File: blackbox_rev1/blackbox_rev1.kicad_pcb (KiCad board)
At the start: 2 copper layers, 16 parts, among them J1 RJ45_LED_Shielded, J2 Molex_uF_SV_06, SW1 SW_Push, SW2 SW_Push, U1 Teensy4.1_DEV-16771, U2 TSR1-2433

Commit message: finish layout design
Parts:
- added J3: Conn_02x08_Counter_Clockwise, blackbox_rev1:timerLED, F.Cu at (89.5, 92.7)
- moved SW1 28.7 mm to (124.2, 95.2)
- moved SW2 28.7 mm to (133.9, 95.2)
- moved C1 22.2 mm to (99.9, 59.9), turned to 0 degrees
- moved C2 14.6 mm to (104.6, 66.6), turned to -90 degrees
- moved C3 9.42 mm to (101.9, 66.6), turned to -90 degrees
- moved U2 8.05 mm to (90.4, 64.0)
- moved Conn1 8.02 mm to (79.2, 57.9)
- moved D3 7.75 mm to (99.7, 70.1), turned to 180 degrees
- moved R3 7.34 mm to (98.8, 66.7)
- moved R1 6.58 mm to (88.8, 70.1), turned to 180 degrees
- moved D1 6.16 mm to (93.0, 70.1), turned to 180 degrees
- moved Conn2 5.11 mm to (62.2, 74.2)
- moved J2 3.11 mm to (112.3, 67.9)
- moved J1 2.77 mm to (139.2, 61.8)
- moved C4 2.39 mm to (113.3, 55.7)
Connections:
- C2 pad 1: +3V3 -> +5V
- C3 pad 1: +3V3 -> +5V
- R3 pad 2: +3V3 -> +5V
- U1 pad 0: Display_A -> Display_D1_Low
- U1 pad 1: Display_B -> Display_D2_Low
- U1 pad 10: unconnected-(U1-Pad10) -> Display_D3_Low
- U1 pad 11: unconnected-(U1-Pad11) -> Display_D4_Low
- U1 pad 2: Display_C -> Display_D
- U1 pad 24: Display_D1_Low -> unconnected-(U1-Pad24)
- U1 pad 25: Display_D2_Low -> unconnected-(U1-Pad25)
- U1 pad 26: Display_D3_Low -> unconnected-(U1-Pad26)
- U1 pad 27: Display_D4_Low -> unconnected-(U1-Pad27)
- U1 pad 28: unconnected-(U1-Pad28) -> Sw_Hour
- U1 pad 29: unconnected-(U1-Pad29) -> Sw_Min
- U1 pad 3: Display_D -> Display_B
- U1 pad 4: Display_E -> Display_G
- U1 pad 5: Display_F -> Display_A
- U1 pad 6: Display_G -> Display_C
- U1 pad 7: Sw_Hour -> Clock_SquareWave
- U1 pad 8: Sw_Min -> Display_F
- U1 pad 9: unconnected-(U1-Pad9) -> Display_E
- U1 pad VIN: unconnected-(U1-PadVIN) -> +5V
- U2 pad 3: +3V3 -> +5V
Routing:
- net +3V3: track 0.00 -> 85.4 mm
- net +5V: track 0.00 -> 36.6 mm
- net Net-(C4-Pad2): track 0.00 -> 36.1 mm, vias 0 -> 1
- net +36V: track 0.00 -> 29.9 mm
- net Display_D1_Low: track 0.00 -> 17.4 mm
- net Display_D2_Low: track 0.00 -> 17.3 mm
- net Display_D: track 0.00 -> 17.1 mm
- net Display_D3_Low: track 0.00 -> 16.5 mm
- net Display_E: track 0.00 -> 16.3 mm
- net Net-(J1-Pad10): track 0.00 -> 16.2 mm
- net Display_D4_Low: track 0.00 -> 15.7 mm
- net Net-(C4-Pad1): track 0.00 -> 14.9 mm
- net Sw_Min: track 0.00 -> 12.3 mm
- net Sw_Hour: track 0.00 -> 12.3 mm
- net Net-(J1-Pad3): track 0.00 -> 9.81 mm
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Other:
- board outline added: 83.8 x 53.3 mm
- board text added: "BlackBox Board,2023 Rev1 Mars Rover Design Team Sanfan Liu"

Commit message: switch 3v3 oki to 5v
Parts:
- moved D3 5.84 mm to (105.5, 70.1)
- moved R3 5.84 mm to (104.6, 66.7)
- moved C2 5.59 mm to (99.1, 66.6)
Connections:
- SW1 pad 1: +3V3 -> GND
- SW2 pad 1: +3V3 -> GND
- U1 pad 3.3V_1: +3V3 -> Net-(U1-Pad3.3V_1)
- U1 pad 3.3V_2: +3V3 -> Net-(U1-Pad3.3V_1)
- U1 pad 3.3V_3: +3V3 -> Net-(U1-Pad3.3V_1)
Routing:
- net +3V3: track 85.4 -> 0.00 mm
- net Net-(U1-Pad3.3V_1): track 0.00 -> 55.8 mm
- net GND: track 0.00 -> 20.7 mm, vias 3 -> 7
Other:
- board text added: "36V"
- board text added: "5V"
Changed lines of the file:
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@@
   (net 1 "+36V")
   (net 2 "GND")
-  (net 3 "+3V3")
+  (net 3 "Net-(U1-Pad3.3V_1)")
   (net 4 "Net-(C4-Pad1)")
   (net 5 "Net-(C4-Pad2)")
@@
   )
   (footprint "LED_SMD:LED_0603_1608Metric_Pad1.05x0.95mm_HandSolder" (layer "F.Cu")
-    (at 99.681 70.104 180)
+    (at 105.523 70.104 180)
     (descr "LED SMD 0603 (1608 Metric), square (rectangular) end terminal, IPC_7351 nominal, (Body size source: http://www.tortai-tech.com/upload/download/2011102023233369053.pdf), generated with kicad-footprint-generator")
     (tags "LED handsolder")
@@
   )
   (footprint "Resistor_SMD:R_0603_1608Metric_Pad0.98x0.95mm_HandSolder" (layer "F.Cu")
-    (at 98.806 66.6985 90)
+    (at 104.648 66.6985 90)
     (descr "Resistor SMD 0603 (1608 Metric), square (rectangular) end terminal, IPC_7351 nominal with elongated pad for handsoldering. (Body size source: IPC-SM-782 page 72, https://www.pcb-3d.com/wordpress/wp-content/uploads/ipc-sm-782a_amendment_1_and_2.pdf), generated with kicad-footprint-generator")
     (tags "resistor handsolder")
@@
     (fp_circle (center 0 0) (end 1.25 0) (layer "F.Fab") (width 0.1) (fill none))
     (pad "1" smd rect (at -3.6 -1.5 180) (size 1.6 1.4) (layers "F.Cu" "F.Paste" "F.Mask")
-      (net 3 "+3V3") (pinfunction "1") (pintype "passive"))
+      (net 2 "GND") (pinfunction "1") (pintype "passive"))
     (pad "1" smd rect (at 3.6 -1.5 180) (size 1.6 1.4) (layers "F.Cu" "F.Paste" "F.Mask")
-      (net 3 "+3V3") (pinfunction "1") (pintype "passive"))
+      (net 2 "GND") (pinfunction "1") (pintype "passive"))
     (pad "2" smd rect (at 3.6 1.5 180) (size 1.6 1.4) (layers "F.Cu" "F.Paste" "F.Mask")
       (net 16 "Sw_Hour") (pinfunction "2") (pintype "passive"))
@@
   )
   (footprint "Capacitor_SMD:C_0603_1608Metric_Pad1.08x0.95mm_HandSolder" (layer "F.Cu")
-    (at 104.648 66.6485 -90)
+    (at 99.06 66.6485 -90)
     (descr "Capacitor SMD 0603 (1608 Metric), square (rectangular) end terminal, IPC_7351 nominal with elongated pad for handsoldering. (Body size source: IPC-SM-782 page 76, https://www.pcb-3d.com/wordpress/wp-content/uploads/ipc-sm-782a_amendment_1_and_2.pdf), generated with kicad-footprint-generator")
     (tags "capacitor handsolder")
@@
     (fp_circle (center 0 0) (end 1.25 0) (layer "F.Fab") (width 0.1) (fill none))
     (pad "1" smd rect (at -3.6 -1.5 180) (size 1.6 1.4) (layers "F.Cu" "F.Paste" "F.Mask")
-      (net 3 "+3V3") (pinfunction "1") (pintype "passive"))
+      (net 2 "GND") (pinfunction "1") (pintype "passive"))
     (pad "1" smd rect (at 3.6 -1.5 180) (size 1.6 1.4) (layers "F.Cu" "F.Paste" "F.Mask")
-      (net 3 "+3V3") (pinfunction "1") (pintype "passive"))
+      (net 2 "GND") (pinfunction "1") (pintype "passive"))
     (pad "2" smd rect (at -3.6 1.5 180) (size 1.6 1.4) (layers "F.Cu" "F.Paste" "F.Mask")
       (net 17 "Sw_Min") (pinfunction "2") (pintype "passive"))
@@
       (net 49 "Display_B") (pinfunction "LRCLK2") (pintype "bidirectional"))
     (pad "3.3V_1" thru_hole circle locked (at 57.15 43.18) (size 1.308 1.308) (drill 0.8) (layers *.Cu *.Mask)
-      (net 3 "+3V3") (pinfunction "3.3V") (pintype "power_in"))
+      (net 3 "Net-(U1-Pad3.3V_1)") (pinfunction "3.3V") (pintype "power_in"))
     (pad "3.3V_2" thru_hole circle locked (at 26.67 27.94) (size 1.308 1.308) (drill 0.8) (layers *.Cu *.Mask)
-      (net 3 "+3V3") (pinfunction "3.3V") (pintype "power_in"))
+      (net 3 "Net-(U1-Pad3.3V_1)") (pinfunction "3.3V") (pintype "power_in"))
     (pad "3.3V_3" thru_hole circle locked (at 67.31 38.1) (size 1.308 1.308) (drill 0.8) (layers *.Cu *.Mask)
-      (net 3 "+3V3") (pinfunction "3.3V") (pintype "power_in"))
+      (net 3 "Net-(U1-Pad3.3V_1)") (pinfunction "3.3V") (pintype "power_in"))
     (pad "4" thru_hole circle locked (at 34.29 43.18) (size 1.308 1.308) (drill 0.8) (layers *.Cu *.Mask)
       (net 34 "Display_G") (pinfunction "BCLK2") (pintype "bidirectional"))
@@
     (effects (font (size 0.95 0.95) (thickness 0.15)) (justify left))
   )
+  (gr_text "5V" (at 102.616 70.104) (layer "F.SilkS")
+    (effects (font (size 1 1) (thickness 0.15)))
+  )
+  (gr_text "36V" (at 96.266 70.104) (layer "F.SilkS")
+    (effects (font (size 1 1) (thickness 0.15)))
+  )
   (dimension (type aligned) (layer "Dwgs.User")
     (pts (xy 140.97 52.324) (xy 140.97 105.664))
@@
   (segment (start 89.408 59.944) (end 99.854 59.944) (width 0.762) (layer "F.Cu") (net 1))
   (segment (start 87.884 65.786) (end 87.884 61.468) (width 0.762) (layer "F.Cu") (net 1))
+  (segment (start 137.502 96.726) (end 137.502 98.386) (width 0.254) (layer "F.Cu") (net 2))
+  (segment (start 120.562 96.726) (end 120.562 98.464) (width 0.254) (layer "F.Cu") (net 2))
+  (segment (start 120.562 98.464) (end 120.65 98.552) (width 0.254) (layer "F.Cu") (net 2))
+  (segment (start 137.502 98.386) (end 137.668 98.552) (width 0.254) (layer "F.Cu") (net 2))
+  (segment (start 120.562 96.726) (end 127.762 96.726) (width 0.254) (layer "F.Cu") (net 2))
+  (segment (start 127.762 96.726) (end 130.302 96.726) (width 0.254) (layer "F.Cu") (net 2))
+  (segment (start 130.302 96.726) (end 137.502 96.726) (width 0.254) (layer "F.Cu") (net 2))
+  (via (at 100.838 69.596) (size 0.8) (drill 0.4) (layers "F.Cu" "B.Cu") (free) (net 2))
+  (via (at 99.06 69.596) (size 0.8) (drill 0.4) (layers "F.Cu" "B.Cu") (free) (net 2))
   (via (at 122.280499 63.695501) (size 0.8) (drill 0.4) (layers "F.Cu" "B.Cu") (net 2))
+  (via (at 137.668 98.552) (size 0.8) (drill 0.4) (layers "F.Cu" "B.Cu") (net 2))
   (via (at 122.407499 59.631501) (size 0.8) (drill 0.4) (layers "F.Cu" "B.Cu") (net 2))
   (via (at 126.090499 62.425501) (size 0.8) (drill 0.4) (layers "F.Cu" "B.Cu") (net 2))
+  (via (at 120.65 98.552) (size 0.8) (drill 0.4) (layers "F.Cu" "B.Cu") (net 2))
   (segment (start 119.38 83.82) (end 124.46 83.82) (width 0.254) (layer "F.Cu") (net 3))
   (segment (start 115.316 83.82) (end 119.38 83.82) (width 0.254) (layer "F.Cu") (net 3))
-  (segment (start 114.3 94.234) (end 116.792 96.726) (width 0.254) (layer "F.Cu") (net 3))
   (segment (start 83.82 80.518) (end 87.122 83.82) (width 0.254) (layer "F.Cu") (net 3))
   (segment (start 87.122 83.82) (end 113.284 83.82) (width 0.254) (layer "F.Cu") (net 3))
@@
   (segment (start 114.3 84.836) (end 113.284 83.82) (width 0.254) (layer "F.Cu") (net 3))
   (segment (start 83.82 73.66) (end 83.82 80.518) (width 0.254) (layer "F.Cu") (net 3))
-  (segment (start 120.562 96.726) (end 127.762 96.726) (width 0.254) (layer "F.Cu") (net 3))
-  (segment (start 116.792 96.726) (end 120.562 96.726) (width 0.254) (layer "F.Cu") (net 3))
-  (segment (start 127.762 96.726) (end 130.302 96.726) (width 0.254) (layer "F.Cu") (net 3))
-  (segment (start 114.3 88.9) (end 114.3 94.234) (width 0.254) (layer "F.Cu") (net 3))
-  (segment (start 130.302 96.726) (end 137.502 96.726) (width 0.254) (layer "F.Cu") (net 3))
   (segment (start 117.281499 65.090501) (end 117.281499 63.820501) (width 0.254) (layer "F.Cu") (net 4))
   (segment (start 117.281499 63.820501) (end 119.821499 61.280501) (width 0.254) (layer "F.Cu") (net 4))
@@
   (segment (start 115.805499 57.470501) (end 117.281499 57.470501) (width 0.25) (layer "B.Cu") (net 5))
   (segment (start 89.709 70.104) (end 92.089 70.104) (width 0.762) (layer "F.Cu") (net 6))
-  (segment (start 98.806 67.611) (end 98.806 70.104) (width 0.254) (layer "F.Cu") (net 7))
+  (segment (start 104.648 67.611) (end 104.648 70.104) (width 0.254) (layer "F.Cu") (net 7))
   (segment (start 118.322538 66.5615) (end 119.580538 65.3035) (width 0.254) (layer "F.Cu") (net 9))
   (segment (start 119.580538 65.3035) (end 129.064498 65.3035) (width 0.254) (layer "F.Cu") (net 9))
@@
     (connect_pads (clearance 0.508))
     (min_thickness 0.254) (filled_areas_thickness no)
-    (fill yes (thermal_gap 0.508) (thermal_bridge_width 0.508))
+    (fill (thermal_gap 0.508) (thermal_bridge_width 0.508))
     (polygon
       (pts
         (xy 140.97 105.664)
-        (xy 57.15 105.918)
+        (xy 57.15 105.664)
         (xy 57.15 52.324)
         (xy 140.97 52.324)

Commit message: hotfix
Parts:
- added G***: LOGO, MRDT_Silkscreens:z_sig_SanfanLiu_sig21.8mmx12.3mm1, F.Cu at (67.3, 96.3)
- Conn1: footprint MRDT_Connectors:Anderson_2_Horizontal_Side_by_Side -> MRDT_Connectors:Square_Anderson_2_H_Side_By_Side
- R1: value 3360 -> 2500
- R3: value 330 -> 200
- moved J1 73.7 mm to (66.3, 51.0), turned to 180 degrees
- moved Conn2 70.0 mm to (129.5, 54.9)
- moved C4 57.1 mm to (60.2, 76.9), turned to 90 degrees
- moved J2 41.0 mm to (72.6, 78.2), turned to -90 degrees
- moved Conn1 35.3 mm to (113.1, 67.9), turned to -90 degrees
- moved D3 31.8 mm to (77.2, 55.6), turned to 0 degrees
- moved R3 27.6 mm to (78.1, 59.0), turned to -90 degrees
- moved C3 22.3 mm to (80.9, 59.1), turned to 90 degrees
- moved C2 17.1 mm to (83.7, 59.1), turned to 90 degrees
- moved R1 15.4 mm to (94.0, 55.6), turned to 0 degrees
- moved D1 14.8 mm to (89.8, 55.6), turned to 0 degrees
- moved C1 9.25 mm to (95.0, 67.8), turned to -90 degrees
- moved U2 3.03 mm to (92.3, 61.7), turned to 180 degrees
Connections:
- net Net-(J1-Pad1) renamed /TX+
- net Net-(J1-Pad3) renamed /TX-
- net Net-(J1-Pad4) renamed /RX+
- net Net-(J1-Pad6) renamed /RX-
- Conn2 pad 1: (no net) -> VBAT
- Conn2 pad 2: (no net) -> GND
- U1 pad VBAT: Net-(Conn2-Pad+V) -> VBAT
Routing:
- net VBAT: track 0.00 -> 64.1 mm
- net +5V: track 36.6 -> 25.7 mm
- net +36V: track 29.9 -> 23.6 mm
- net GND: track 20.7 -> 17.3 mm
- net Net-(C4-Pad2): track 36.1 -> 38.6 mm
- net /RX-: track 6.64 -> 9.14 mm
- net /RX+: track 7.07 -> 9.26 mm
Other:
- board size 83.8 x 53.3 mm -> 84.1 x 78.7 mm
- board text added: "Keep Out Zone"

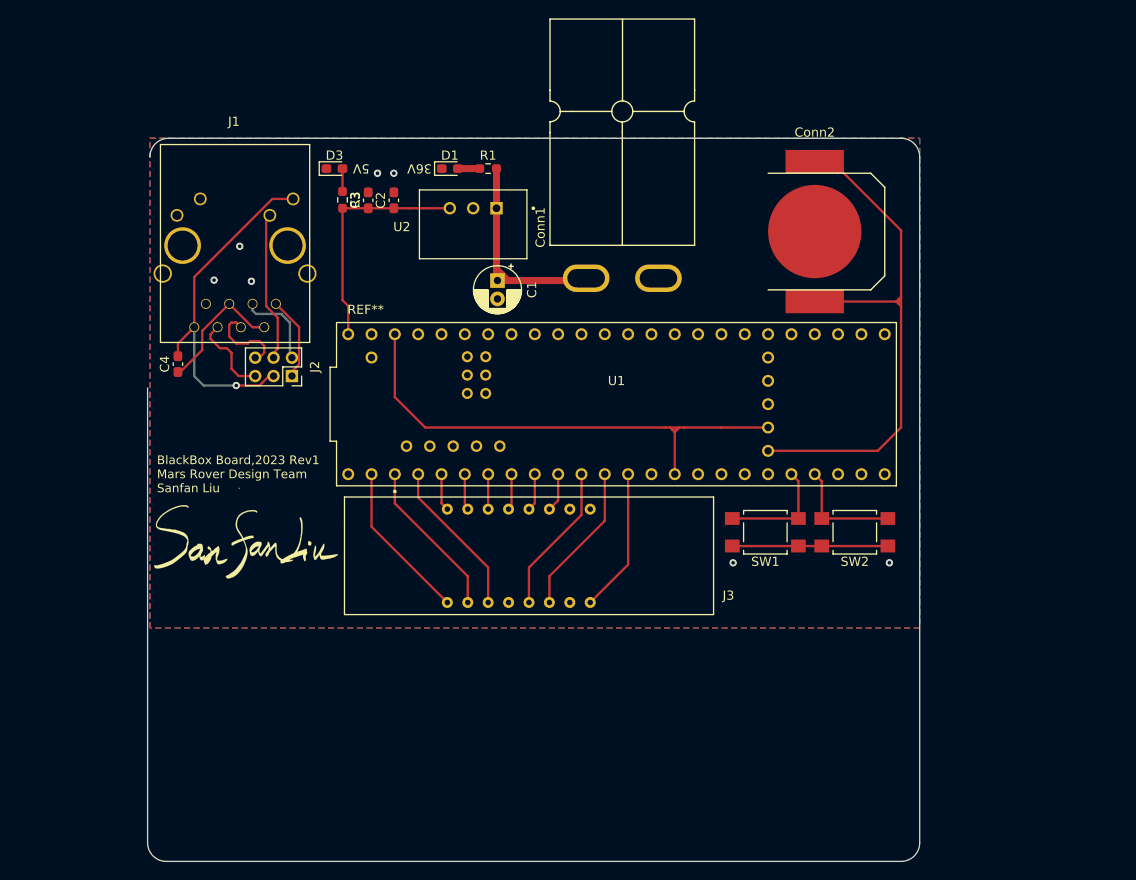
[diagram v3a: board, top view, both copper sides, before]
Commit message: change connector direction
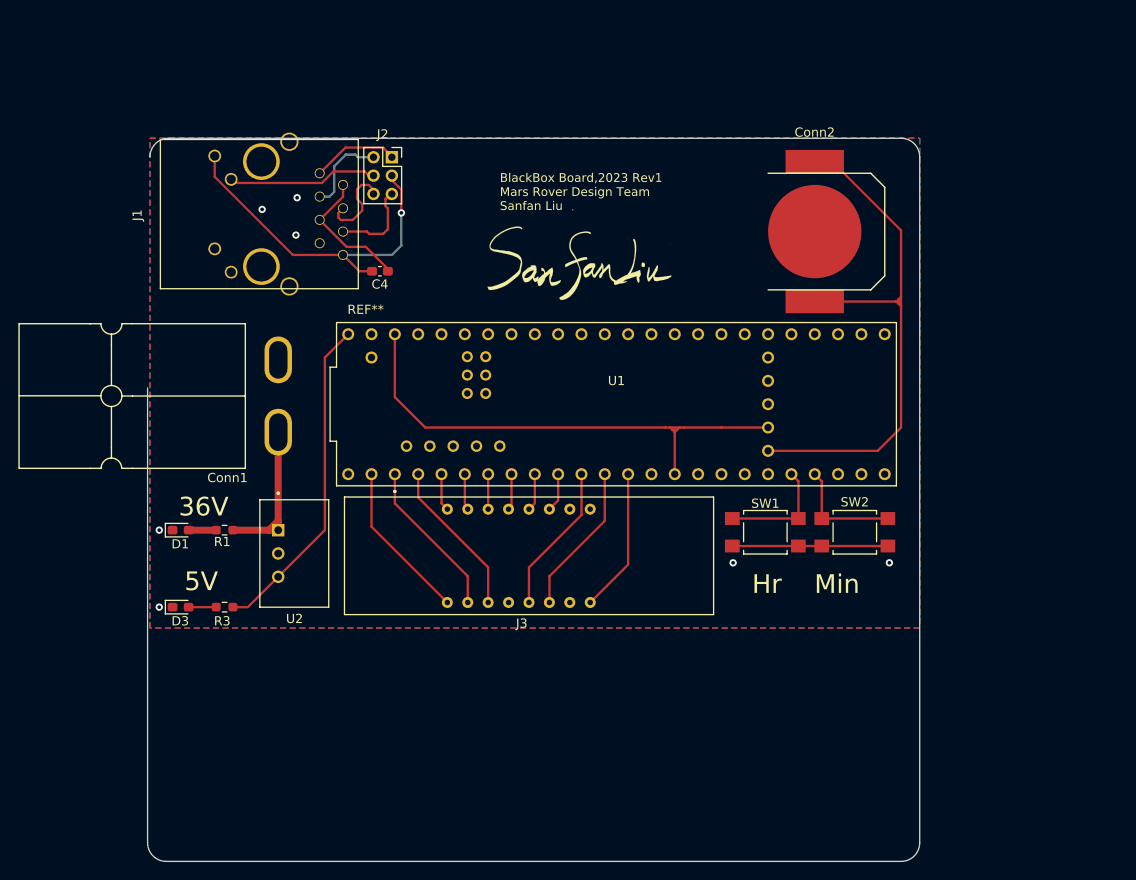
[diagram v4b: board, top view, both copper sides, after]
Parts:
- removed C1: 22uF, Capacitor_THT:CP_Radial_D5.0mm_P2.00mm
- removed C2: 10uF, Capacitor_SMD:C_0603_1608Metric_Pad1.08x0.95mm_HandSolder
- removed C3: 1uF, Capacitor_SMD:C_0603_1608Metric_Pad1.08x0.95mm_HandSolder
- moved D3 50.6 mm to (60.5, 103.4)
- moved D1 49.1 mm to (60.5, 95.0)
- moved R1 48.7 mm to (65.3, 95.0)
- moved G*** 47.3 mm to (103.6, 65.9)
- moved R3 46.2 mm to (65.3, 103.4), turned to 0 degrees
- moved Conn1 42.3 mm to (71.5, 75.9), turned to 0 degrees
- moved U2 40.8 mm to (72.9, 97.5), turned to -90 degrees
- moved J2 26.2 mm to (83.5, 54.4), turned to 0 degrees
- moved C4 24.2 mm to (82.2, 66.8), turned to 180 degrees
- moved J1 13.9 mm to (56.3, 60.7), turned to -90 degrees
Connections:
- Conn2 pad 1: VBAT -> (no net)
- Conn2 pad 2: GND -> (no net)
- U1 pad VBAT: VBAT -> Net-(Conn2-Pad+V)
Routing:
- net VBAT: track 64.1 -> 0.00 mm
- net Net-(Conn2-Pad+V): track 0.00 -> 64.1 mm
- net +5V: track 25.7 -> 35.9 mm
- net +36V: track 23.6 -> 17.0 mm
- net /TX-: track 9.63 -> 10.3 mm
- net Net-(D1-Pad2): track 2.38 -> 3.00 mm
- net Net-(D3-Pad2): track 2.49 -> 3.00 mm
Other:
- board text added: "Hr Min"
